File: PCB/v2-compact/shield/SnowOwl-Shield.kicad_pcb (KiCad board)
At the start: 4 copper layers, 60 x 85 mm, 1 part, among them J1 STACK_2x10

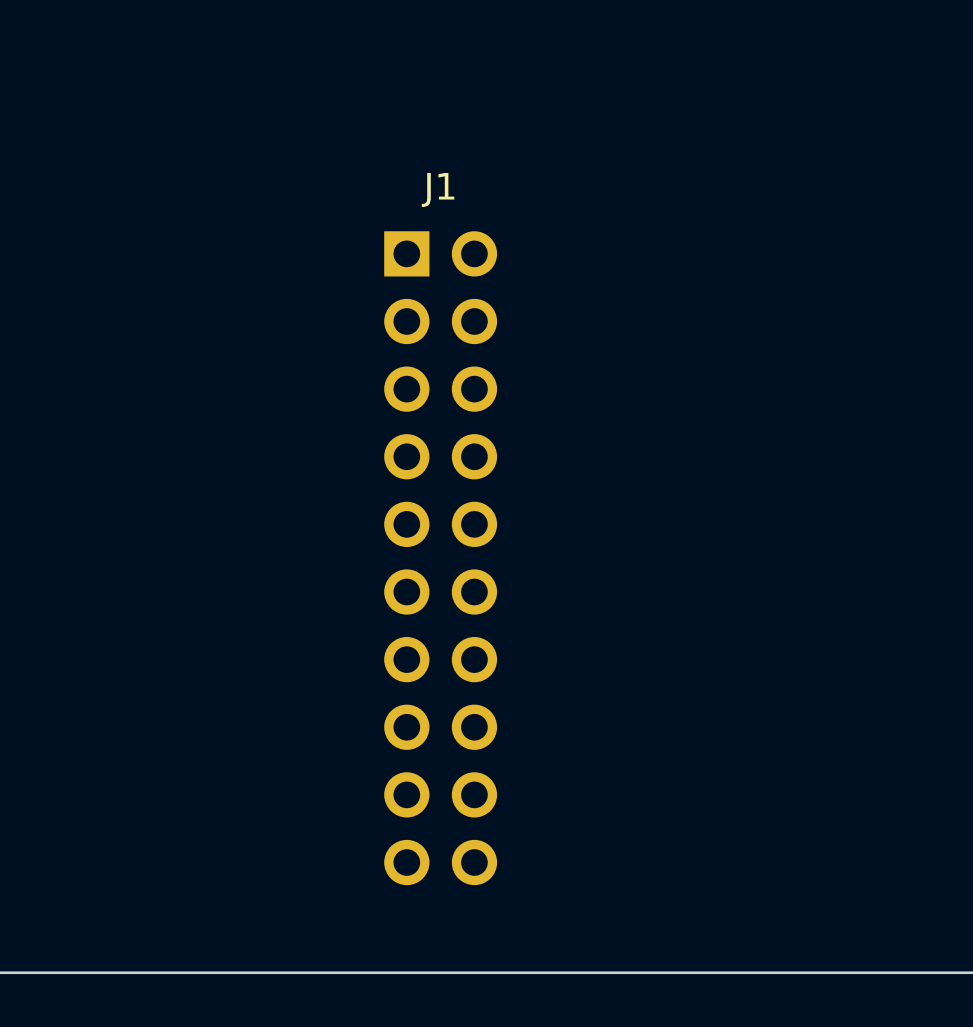
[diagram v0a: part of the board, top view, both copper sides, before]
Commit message: PCB: rework main board to phone-style layout; J1 -> horizontal strip
Main board (per feedback) is now a phone-style split — front is pure UI, back
carries the electronics:
- FRONT: status LEDs at the very top (above the display), TFT rotated to
  LANDSCAPE (sideways), nav buttons below it and moved down. Same feel as the
  ESP32-DIV, sideways screen.
- BACK: ESP32-S3 behind the display, microSD beside it, power + USB-C at the
  bottom-centre edge like a phone.

To keep the centre column free for the landscape display and the bottom-centre
USB-C, J1 is reoriented from a vertical 2x10 to a HORIZONTAL 10x2 strip in the
lower-centre. J1 is the shared mating datum, so the shield's J1 moves to match;
the shield's RV1106 / HTRC110 / bulk-cap zones shift to sit above/below the new
strip (SPI spine still runs north from it). Every v1 capability unchanged.

Updated both .kicad_pcb, both floorplan SVGs, both schematics' zone specs, and
PLACEMENT.md. Verified: files parse, J1 clears all zones, no same-side overlaps.

Co-Authored-By: Claude <noreply@anthropic.com>
Claude-Session: https://claude.ai/code/session_017BEAKBRVwbUCc7Sa2o3Ye7
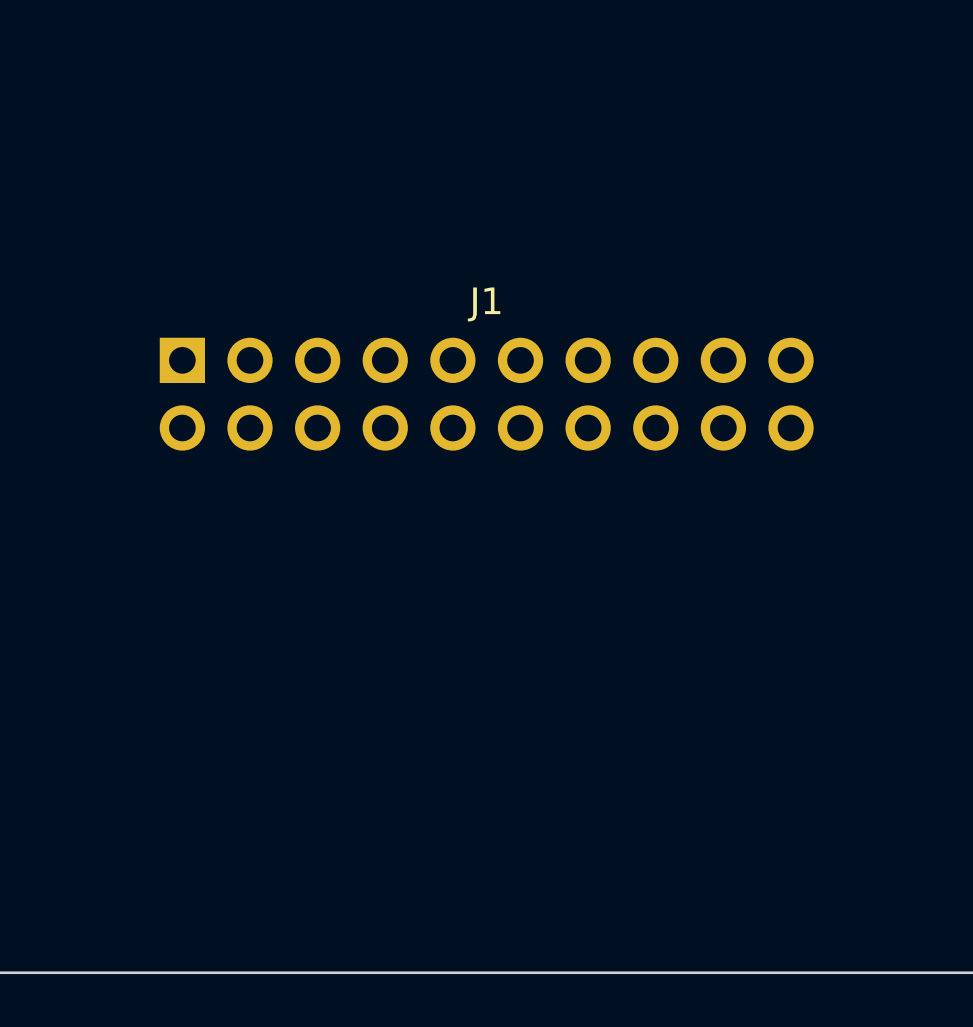
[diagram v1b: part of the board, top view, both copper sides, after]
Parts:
- moved J1 9.33 mm to (48.6, 92.0)
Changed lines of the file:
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@@
   (gr_text "ESP32-C5 + LDO (U.FL)" (at 70.8 62.0) (layer "User.1")
     (effects (font (size 1.1 1.1) (thickness 0.18)) (justify left)))
-  (gr_rect (start 33.0 84.0) (end 51.0 92.0) (stroke (width 0.15) (type solid)) (fill none) (layer "User.1"))
-  (gr_text "iButton / 1-Wire" (at 33.8 86.0) (layer "User.1")
+  (gr_rect (start 33.0 83.0) (end 48.0 90.0) (stroke (width 0.15) (type solid)) (fill none) (layer "User.1"))
+  (gr_text "iButton / 1-Wire" (at 33.8 85.0) (layer "User.1")
     (effects (font (size 1.1 1.1) (thickness 0.18)) (justify left)))
   (gr_rect (start 34.0 36.0) (end 50.0 56.0) (stroke (width 0.12) (type solid)) (fill none) (layer "User.2"))
@@
   (gr_text "(BACK) nRF24 #3" (at 70.8 38.0) (layer "User.2")
     (effects (font (size 1.1 1.1) (thickness 0.18)) (justify left)))
-  (gr_rect (start 33.0 70.0) (end 57.0 96.0) (stroke (width 0.12) (type solid)) (fill none) (layer "User.2"))
-  (gr_text "(BACK) HTRC110 125kHz + coil" (at 33.8 72.0) (layer "User.2")
+  (gr_rect (start 33.0 64.0) (end 57.0 90.0) (stroke (width 0.12) (type solid)) (fill none) (layer "User.2"))
+  (gr_text "(BACK) HTRC110 125kHz + coil" (at 33.8 66.0) (layer "User.2")
     (effects (font (size 1.1 1.1) (thickness 0.18)) (justify left)))
-  (gr_rect (start 60.0 70.0) (end 87.0 110.0) (stroke (width 0.12) (type solid)) (fill none) (layer "User.2"))
-  (gr_text "(BACK) RV1106 Luckfox SoM" (at 60.8 72.0) (layer "User.2")
+  (gr_rect (start 61.0 64.0) (end 87.0 90.0) (stroke (width 0.12) (type solid)) (fill none) (layer "User.2"))
+  (gr_text "(BACK) RV1106 Luckfox SoM" (at 61.8 66.0) (layer "User.2")
     (effects (font (size 1.1 1.1) (thickness 0.18)) (justify left)))
-  (gr_rect (start 33.0 96.0) (end 57.0 110.0) (stroke (width 0.12) (type solid)) (fill none) (layer "User.2"))
+  (gr_rect (start 33.0 96.0) (end 60.0 112.0) (stroke (width 0.12) (type solid)) (fill none) (layer "User.2"))
   (gr_text "(BACK) bulk caps / power" (at 33.8 98.0) (layer "User.2")
     (effects (font (size 1.1 1.1) (thickness 0.18)) (justify left)))
@@
   (gr_text "C5 U.FL >" (at 87.5 70.0) (layer "Cmts.User")
     (effects (font (size 1.0 1.0) (thickness 0.15)) (justify left)))
-  (gr_text "RV1106 USB-C >" (at 87.5 102.0) (layer "Cmts.User")
+  (gr_text "RV1106 USB-C >" (at 87.5 82.0) (layer "Cmts.User")
     (effects (font (size 1.0 1.0) (thickness 0.15)) (justify left)))
-  (gr_text "< LF coil" (at 30.5 85.0) (layer "Cmts.User")
+  (gr_text "< LF coil" (at 30.5 80.0) (layer "Cmts.User")
     (effects (font (size 1.0 1.0) (thickness 0.15)) (justify left)))
   (footprint "SnowOwl:StackHeader_2x10" (layer "F.Cu")
-    (at 57.0 88.0)
+    (at 48.57 92.0)
     (descr "SnowOwl 2x10 2.54mm inter-board stack header (shared datum)")
     (attr through_hole)
-    (fp_text reference "J1" (at 1.27 -2.5) (layer "F.SilkS")
+    (fp_text reference "J1" (at 11.43 -2.2) (layer "F.SilkS")
       (effects (font (size 1 1) (thickness 0.15))))
-    (fp_text value "STACK_2x10" (at 1.27 25.4) (layer "F.Fab")
+    (fp_text value "STACK_2x10" (at 11.43 4.7) (layer "F.Fab")
       (effects (font (size 1 1) (thickness 0.15))))
     (pad "1" thru_hole rect (at 0.0 0.0) (size 1.7 1.7) (drill 1.0) (layers "*.Cu" "*.Mask"))
     (pad "2" thru_hole oval (at 2.54 0.0) (size 1.7 1.7) (drill 1.0) (layers "*.Cu" "*.Mask"))
-    (pad "3" thru_hole oval (at 0.0 2.54) (size 1.7 1.7) (drill 1.0) (layers "*.Cu" "*.Mask"))
-    (pad "4" thru_hole oval (at 2.54 2.54) (size 1.7 1.7) (drill 1.0) (layers "*.Cu" "*.Mask"))
-    (pad "5" thru_hole oval (at 0.0 5.08) (size 1.7 1.7) (drill 1.0) (layers "*.Cu" "*.Mask"))
-    (pad "6" thru_hole oval (at 2.54 5.08) (size 1.7 1.7) (drill 1.0) (layers "*.Cu" "*.Mask"))
-    (pad "7" thru_hole oval (at 0.0 7.62) (size 1.7 1.7) (drill 1.0) (layers "*.Cu" "*.Mask"))
-    (pad "8" thru_hole oval (at 2.54 7.62) (size 1.7 1.7) (drill 1.0) (layers "*.Cu" "*.Mask"))
-    (pad "9" thru_hole oval (at 0.0 10.16) (size 1.7 1.7) (drill 1.0) (layers "*.Cu" "*.Mask"))
-    (pad "10" thru_hole oval (at 2.54 10.16) (size 1.7 1.7) (drill 1.0) (layers "*.Cu" "*.Mask"))
-    (pad "11" thru_hole oval (at 0.0 12.7) (size 1.7 1.7) (drill 1.0) (layers "*.Cu" "*.Mask"))
-    (pad "12" thru_hole oval (at 2.54 12.7) (size 1.7 1.7) (drill 1.0) (layers "*.Cu" "*.Mask"))
-    (pad "13" thru_hole oval (at 0.0 15.24) (size 1.7 1.7) (drill 1.0) (layers "*.Cu" "*.Mask"))
-    (pad "14" thru_hole oval (at 2.54 15.24) (size 1.7 1.7) (drill 1.0) (layers "*.Cu" "*.Mask"))
-    (pad "15" thru_hole oval (at 0.0 17.78) (size 1.7 1.7) (drill 1.0) (layers "*.Cu" "*.Mask"))
-    (pad "16" thru_hole oval (at 2.54 17.78) (size 1.7 1.7) (drill 1.0) (layers "*.Cu" "*.Mask"))
-    (pad "17" thru_hole oval (at 0.0 20.32) (size 1.7 1.7) (drill 1.0) (layers "*.Cu" "*.Mask"))
-    (pad "18" thru_hole oval (at 2.54 20.32) (size 1.7 1.7) (drill 1.0) (layers "*.Cu" "*.Mask"))
-    (pad "19" thru_hole oval (at 0.0 22.86) (size 1.7 1.7) (drill 1.0) (layers "*.Cu" "*.Mask"))
-    (pad "20" thru_hole oval (at 2.54 22.86) (size 1.7 1.7) (drill 1.0) (layers "*.Cu" "*.Mask"))
+    (pad "3" thru_hole oval (at 5.08 0.0) (size 1.7 1.7) (drill 1.0) (layers "*.Cu" "*.Mask"))
+    (pad "4" thru_hole oval (at 7.62 0.0) (size 1.7 1.7) (drill 1.0) (layers "*.Cu" "*.Mask"))
+    (pad "5" thru_hole oval (at 10.16 0.0) (size 1.7 1.7) (drill 1.0) (layers "*.Cu" "*.Mask"))
+    (pad "6" thru_hole oval (at 12.7 0.0) (size 1.7 1.7) (drill 1.0) (layers "*.Cu" "*.Mask"))
+    (pad "7" thru_hole oval (at 15.24 0.0) (size 1.7 1.7) (drill 1.0) (layers "*.Cu" "*.Mask"))
+    (pad "8" thru_hole oval (at 17.78 0.0) (size 1.7 1.7) (drill 1.0) (layers "*.Cu" "*.Mask"))
+    (pad "9" thru_hole oval (at 20.32 0.0) (size 1.7 1.7) (drill 1.0) (layers "*.Cu" "*.Mask"))
+    (pad "10" thru_hole oval (at 22.86 0.0) (size 1.7 1.7) (drill 1.0) (layers "*.Cu" "*.Mask"))
+    (pad "11" thru_hole oval (at 0.0 2.54) (size 1.7 1.7) (drill 1.0) (layers "*.Cu" "*.Mask"))
+    (pad "12" thru_hole oval (at 2.54 2.54) (size 1.7 1.7) (drill 1.0) (layers "*.Cu" "*.Mask"))
+    (pad "13" thru_hole oval (at 5.08 2.54) (size 1.7 1.7) (drill 1.0) (layers "*.Cu" "*.Mask"))
+    (pad "14" thru_hole oval (at 7.62 2.54) (size 1.7 1.7) (drill 1.0) (layers "*.Cu" "*.Mask"))
+    (pad "15" thru_hole oval (at 10.16 2.54) (size 1.7 1.7) (drill 1.0) (layers "*.Cu" "*.Mask"))
+    (pad "16" thru_hole oval (at 12.7 2.54) (size 1.7 1.7) (drill 1.0) (layers "*.Cu" "*.Mask"))
+    (pad "17" thru_hole oval (at 15.24 2.54) (size 1.7 1.7) (drill 1.0) (layers "*.Cu" "*.Mask"))
+    (pad "18" thru_hole oval (at 17.78 2.54) (size 1.7 1.7) (drill 1.0) (layers "*.Cu" "*.Mask"))
+    (pad "19" thru_hole oval (at 20.32 2.54) (size 1.7 1.7) (drill 1.0) (layers "*.Cu" "*.Mask"))
+    (pad "20" thru_hole oval (at 22.86 2.54) (size 1.7 1.7) (drill 1.0) (layers "*.Cu" "*.Mask"))
   )
-  (gr_text "J1 STACK (datum: shared X/Y on both boards)" (at 55.0 112.5) (layer "Cmts.User")
+  (gr_text "J1 STACK (datum: shared X/Y on both boards)" (at 48.57 97.0) (layer "Cmts.User")
     (effects (font (size 1.0 1.0) (thickness 0.15)) (justify left)))
 )
